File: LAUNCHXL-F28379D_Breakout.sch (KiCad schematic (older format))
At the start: 20 parts, among them IC1 LM358N, Q1 100V/17A, Q2 100V/17A, Q3 100V/17A, Q4 100V/17A, Q5 100V/17A, Q6 100V/17A

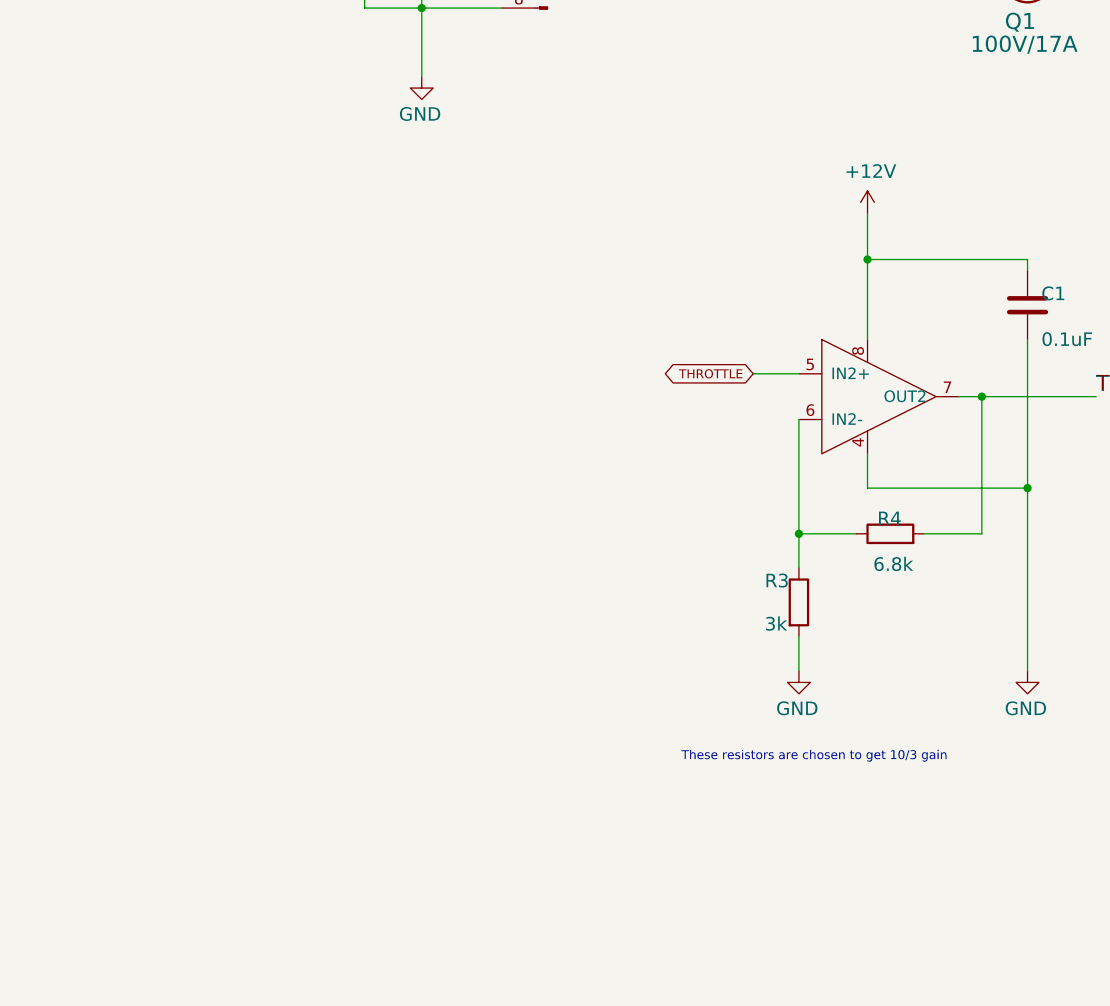
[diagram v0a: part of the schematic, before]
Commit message: Changed to diff op amp with single sided supply
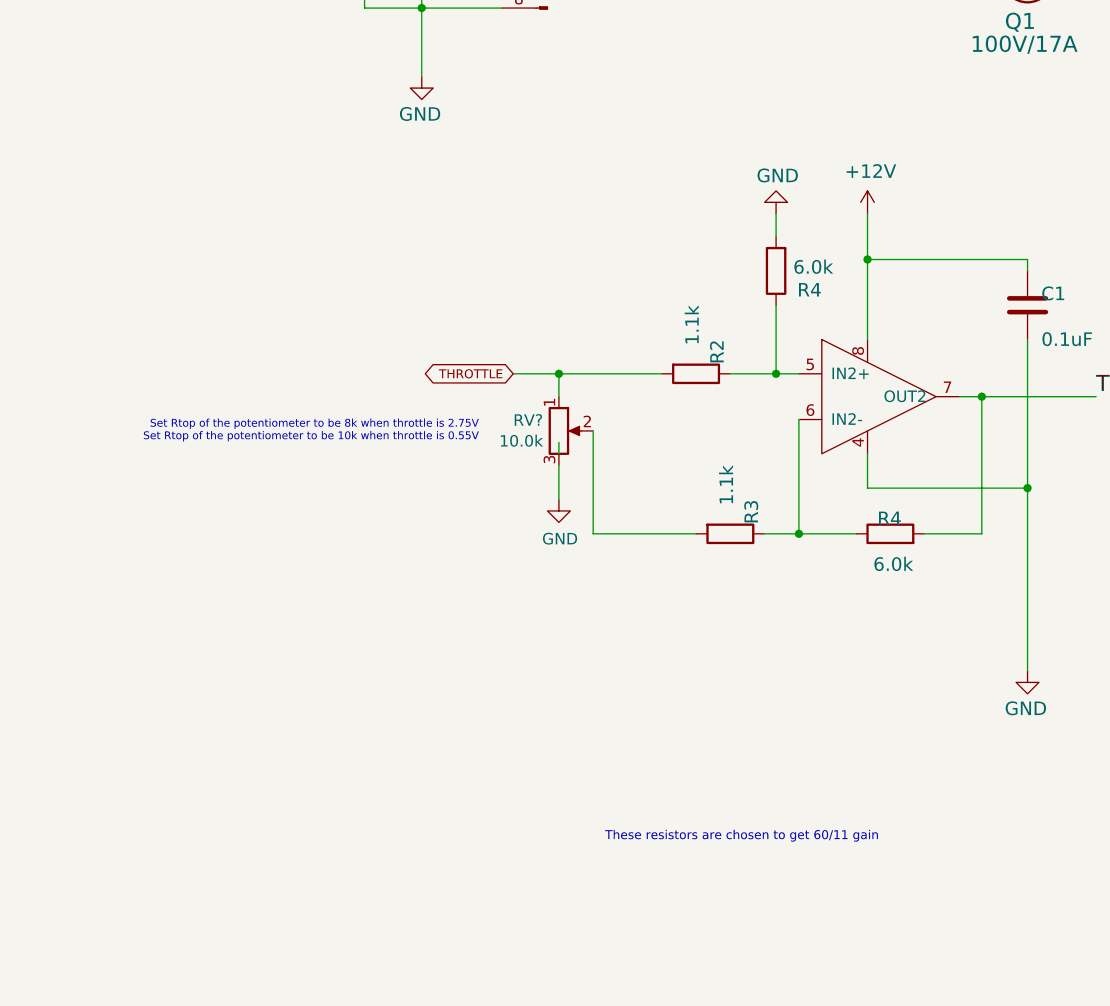
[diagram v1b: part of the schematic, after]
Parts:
- added R2: 1.1k, Resistor_SMD:R_0805_2012Metric_Pad1.15x1.40mm_HandSolder, symbol Device:R
- added R4: 6.0k, Resistor_SMD:R_0805_2012Metric_Pad1.15x1.40mm_HandSolder, symbol Device:R
- added RV?: 10.0k, symbol Device:R_POT
- R3: value 3k -> 1.1k
- R4: value 6.8k -> 6.0k
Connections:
- net GND: now also R4.2, RV?.3; no longer R3.2
- net THROTTLE: now also R2.2, RV?.1; no longer IC1.5 (IN2+)
- new net: IC1.5 (IN2+), R2.1, R4.1
- new net: R3.2, RV?.2
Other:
- note added: "Set Rtop of the potentiometer to be 8k when throttle is 2.75V\nSet Rtop of the potentiometer to be 10k when throttle is 0.55V"
- note added: "These resistors are chosen to get 60/11 gain"
- note removed: "These resistors are chosen to get 10/3 gain"
- moved on the sheet: R3
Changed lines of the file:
@@
 EESchema Schematic File Version 4
-LIBS:PCB_2020-cache
 EELAYER 30 0
 EELAYER END
@@
 AR Path="/5DF27AC1/D7A12E91" Ref="R4"  Part="1"
 F 0 "R4" V 4800 4050 59  0000 L BNN
-F 1 "6.8k" V 4600 4000 59  0000 L BNN
+F 1 "6.0k" V 4600 4000 59  0000 L BNN
 F 2 "Resistor_SMD:R_0805_2012Metric_Pad1.15x1.40mm_HandSolder" H 4700 4100 50  0001 C CNN
 F 3 "" H 4700 4100 50  0001 C CNN
@@
 F 3 "" H 6700 2400 50  0001 C CNN
 	1    6700 2400
-	1    0    0    -1
-$EndComp
-$Comp
-L power:GND #GND6
-U 1 1 6DBAC010
-P 4300 4700
-AR Path="/6DBAC010" Ref="#GND6"  Part="1"
-AR Path="/5DD5E236/6DBAC010" Ref="#GND6"  Part="1"
-AR Path="/5DF27AC1/6DBAC010" Ref="#GND06"  Part="1"
-F 0 "#GND06" H 4300 4700 50  0001 C CNN
-F 1 "GND" H 4200 4500 59  0000 L BNN
-F 2 "" H 4300 4700 50  0001 C CNN
-F 3 "" H 4300 4700 50  0001 C CNN
-	1    4300 4700
 	1    0    0    -1
 $EndComp
@@
 L Device:R R3
 U 1 1 D43D5682
-P 4300 4400
+P 4000 4100
 AR Path="/D43D5682" Ref="R3"  Part="1"
 AR Path="/5DD5E236/D43D5682" Ref="R3"  Part="1"
 AR Path="/5DF27AC1/D43D5682" Ref="R3"  Part="1"
-F 0 "R3" H 4150 4459 59  0000 L BNN
-F 1 "3k" H 4150 4270 59  0000 L BNN
-F 2 "Resistor_SMD:R_0805_2012Metric_Pad1.15x1.40mm_HandSolder" H 4300 4400 50  0001 C CNN
-F 3 "" H 4300 4400 50  0001 C CNN
-	1    4300 4400
-	1    0    0    -1
-$EndComp
-Wire Wire Line
-	4300 4100 4300 4250
-Wire Wire Line
-	4300 4550 4300 4700
+F 0 "R3" H 3850 4159 59  0000 L BNN
+F 1 "1.1k" H 3700 4050 59  0000 L BNN
+F 2 "Resistor_SMD:R_0805_2012Metric_Pad1.15x1.40mm_HandSolder" H 4000 4100 50  0001 C CNN
+F 3 "" H 4000 4100 50  0001 C CNN
+	1    4000 4100
+	0    1    1    0
+$EndComp
+Wire Wire Line
+	4300 4100 4150 4100
 Wire Wire Line
 	4800 1300 4800 1350
@@
 Wire Wire Line
 	5300 3250 5300 3900
-Wire Wire Line
-	4100 3400 4300 3400
 Wire Wire Line
 	4600 3750 4600 3900
@@
 Text Notes 7700 4150 2    39   ~ 0
 resistor code is either 195 - 1.9M ohms\nor 561 - 560 ohms
-Text Notes 4950 5100 2    39   ~ 0
-These resistors are chosen to get 10/3 gain
+Text Notes 4650 5450 2    39   ~ 0
+These resistors are chosen to get 60/11 gain
 Text Label 6000 1700 0    70   ~ 0
 INPUT_B+
@@
 	0    1    1    0
 $EndComp
-Text GLabel 4100 3400 0    39   BiDi ~ 0
+Text GLabel 3050 3400 0    39   BiDi ~ 0
 THROTTLE
+$Comp
+L Device:R R?
+U 1 1 5F860B43
+P 3850 3400
+AR Path="/5F860B43" Ref="R?"  Part="1"
+AR Path="/5DD5E236/5F860B43" Ref="R?"  Part="1"
+AR Path="/5DF27AC1/5F860B43" Ref="R2"  Part="1"
+F 0 "R2" H 3700 3459 59  0000 L BNN
+F 1 "1.1k" H 3550 3350 59  0000 L BNN
+F 2 "Resistor_SMD:R_0805_2012Metric_Pad1.15x1.40mm_HandSolder" H 3850 3400 50  0001 C CNN
+F 3 "" H 3850 3400 50  0001 C CNN
+	1    3850 3400
+	0    1    1    0
+$EndComp
+Wire Wire Line
+	4000 3400 4200 3400
+Wire Wire Line
+	4200 3400 4200 3100
+Connection ~ 4200 3400
+Wire Wire Line
+	4200 3400 4300 3400
+$Comp
+L Device:R R?
+U 1 1 5F869B9B
+P 4200 2950
+AR Path="/5F869B9B" Ref="R?"  Part="1"
+AR Path="/5DD5E236/5F869B9B" Ref="R?"  Part="1"
+AR Path="/5DF27AC1/5F869B9B" Ref="R4"  Part="1"
+F 0 "R4" H 4000 3000 59  0000 L BNN
+F 1 "6.0k" H 3950 2900 59  0000 L BNN
+F 2 "Resistor_SMD:R_0805_2012Metric_Pad1.15x1.40mm_HandSolder" H 4200 2950 50  0001 C CNN
+F 3 "" H 4200 2950 50  0001 C CNN
+	1    4200 2950
+	-1   0    0    1
+$EndComp
+Wire Wire Line
+	4200 2700 4200 2800
+$Comp
+L power:GND #GND?
+U 1 1 5F86CB5F
+P 4200 2700
+AR Path="/5F86CB5F" Ref="#GND?"  Part="1"
+AR Path="/5DD5E236/5F86CB5F" Ref="#GND?"  Part="1"
+AR Path="/5DF27AC1/5F86CB5F" Ref="#GND?"  Part="1"
+F 0 "#GND?" H 4200 2700 50  0001 C CNN
+F 1 "GND" H 4100 2500 59  0000 L BNN
+F 2 "" H 4200 2700 50  0001 C CNN
+F 3 "" H 4200 2700 50  0001 C CNN
+	1    4200 2700
+	-1   0    0    1
+$EndComp
+$Comp
+L Device:R_POT RV?
+U 1 1 5F99BDE7
+P 3250 3650
+F 0 "RV?" H 3181 3696 50  0000 R CNN
+F 1 "10.0k" H 3181 3605 50  0000 R CNN
+F 2 "" H 3250 3650 50  0001 C CNN
+F 3 "~" H 3250 3650 50  0001 C CNN
+	1    3250 3650
+	1    0    0    -1
+$EndComp
+Wire Wire Line
+	3400 4100 3850 4100
+Wire Wire Line
+	3250 3700 3250 3750
+$Comp
+L power:GND #PWR?
+U 1 1 5F9A52EE
+P 3250 3950
+F 0 "#PWR?" H 3250 3700 50  0001 C CNN
+F 1 "GND" H 3255 3777 50  0000 C CNN
+F 2 "" H 3250 3950 50  0001 C CNN
+F 3 "" H 3250 3950 50  0001 C CNN
+	1    3250 3950
+	1    0    0    -1
+$EndComp
+Wire Wire Line
+	3400 3650 3400 4100
+Wire Wire Line
+	3050 3400 3250 3400
+Wire Wire Line
+	3250 3400 3250 3500
+Connection ~ 3250 3400
+Wire Wire Line
+	3250 3400 3700 3400
+Wire Wire Line
+	3250 3800 3250 3950
+Text Notes 2900 3700 2    34   ~ 0
+Set Rtop of the potentiometer to be 8k when throttle is 2.75V\nSet Rtop of the potentiometer to be 10k when throttle is 0.55V
 $EndSCHEMATC
